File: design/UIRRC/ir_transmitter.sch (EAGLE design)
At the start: 9 parts, among them IC1 TSOP38438, U1 ESP32-WROOM-32E_(16MB)

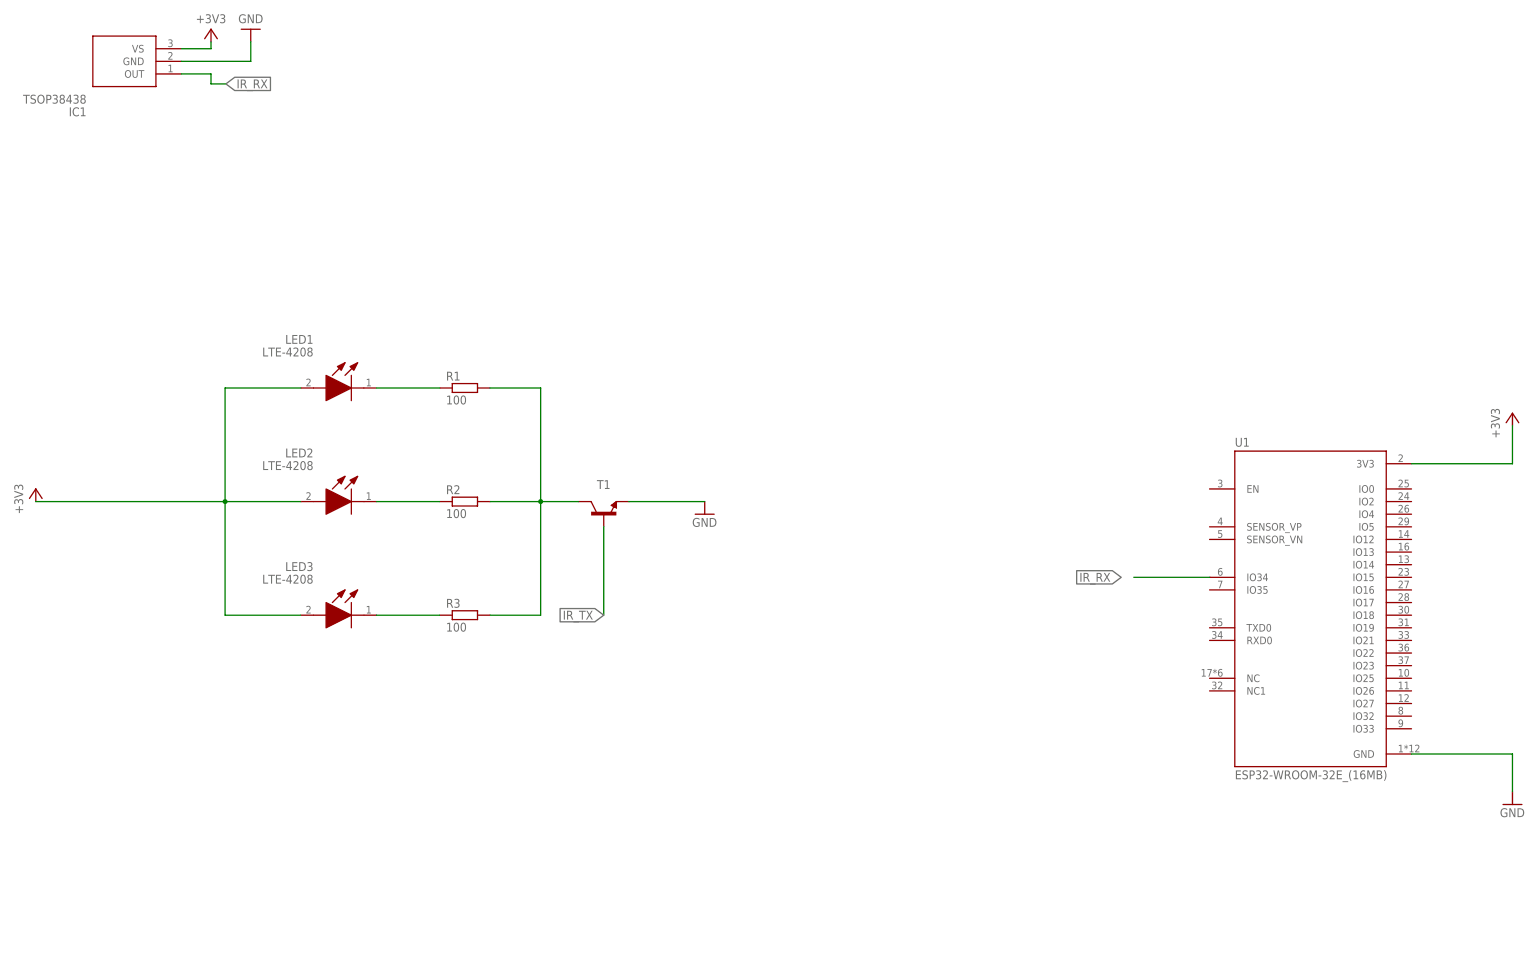
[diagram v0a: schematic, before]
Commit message: Fixes #4
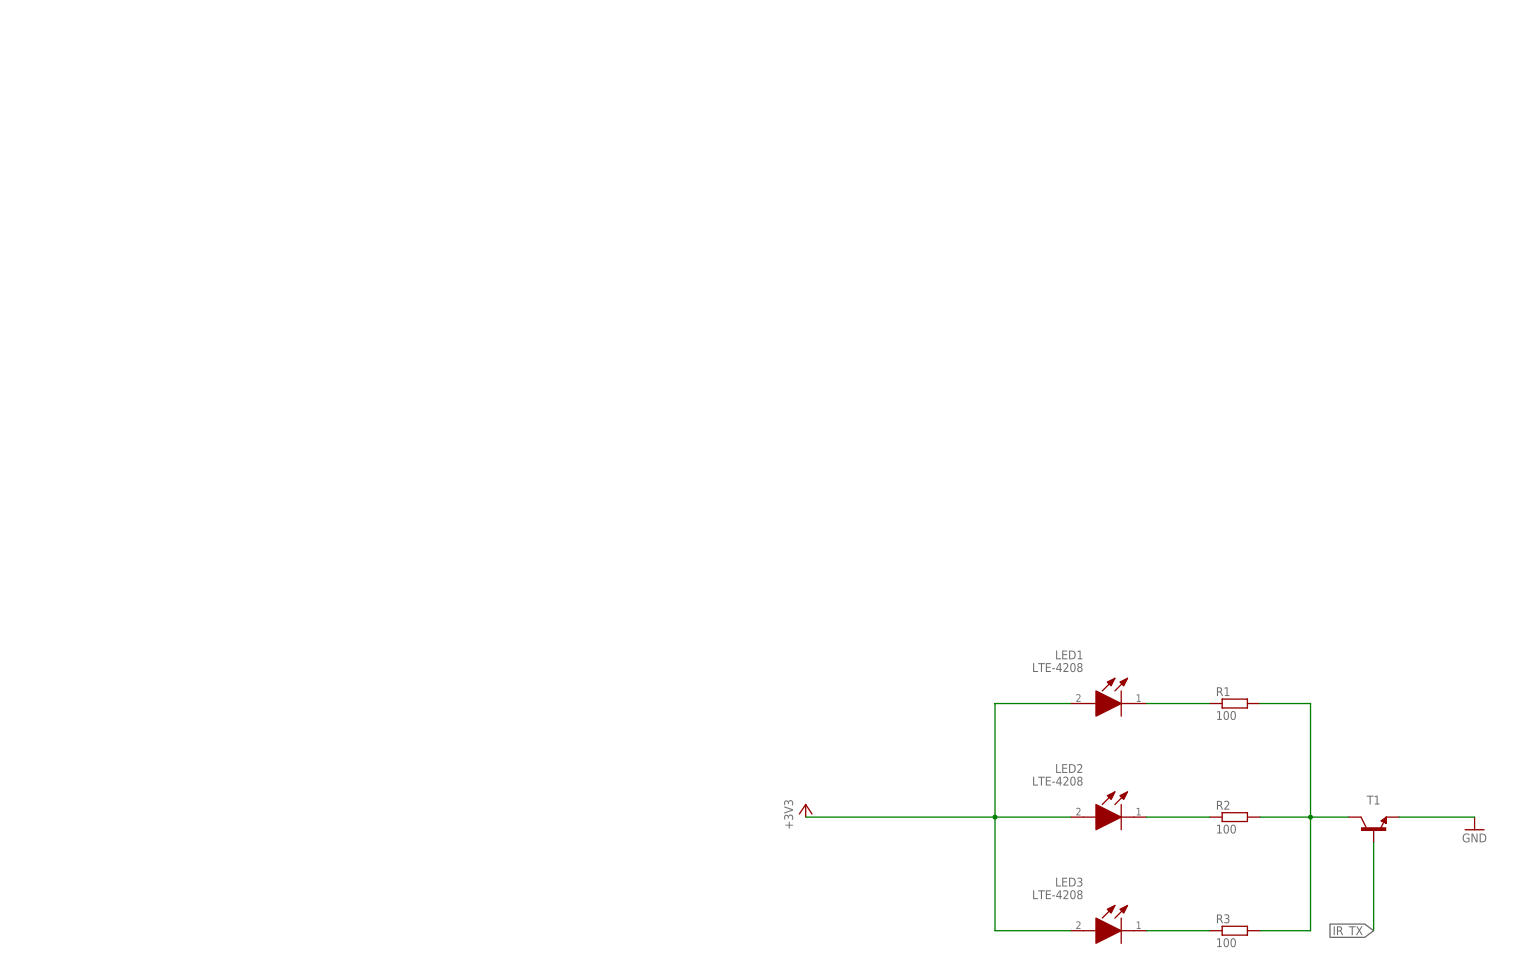
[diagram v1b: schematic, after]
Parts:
- removed IC1: TSOP38438, TSOP38438:TSOP38438
- removed U1: ESP32-WROOM-32E_(16MB), ESP32-WROOM-32E__16MB_:ESP32-WROOM-32E_(16MB)
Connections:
- removed net IR_RX: IC1.OUT, U1.IO34
- net +3V3: no longer IC1.VS, U1.3V3
- net GND: no longer IC1.GND, U1.GND
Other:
- moved on the sheet: LED1, LED2, LED3, R1, R2, R3, T1
